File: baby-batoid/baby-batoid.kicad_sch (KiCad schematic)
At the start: 21 parts, among them J1 USB_C_Receptacle_USB2.0, U1 STM32F072CBT6, U2 PRTR5V0U2X, U3 XC6206PxxxMR-Regulator_Linear

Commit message: built baby batoid :D
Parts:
- added D1, D10, D11, D12, D13, D14, D15, D16, D17, D18, D19, D2, D20, D21, D22, D23, D24, D25, D26, D27, D28, D29, D3, D4, D5, D6, D7, D8, D9: D_Small, Diode_SMD:D_SOD-123, symbol Device:D_Small
- added MX1, MX10, MX11, MX12, MX13, MX14, MX15, MX16, MX17, MX18, MX19, MX2, MX20, MX21, MX22, MX23, MX24, MX25, MX26, MX27, MX28, MX29, MX3, MX4, MX5, MX6, MX7, MX8, MX9: MX_SW_HS, marbastlib-mx:SW_MX_HS_CPG151101S11_1u, symbol marbastlib-mx:MX_SW_HS_CPG151101S11
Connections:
- net A0 renamed ROW3
- net ROW3: now also D13.2 (A), D14.2 (A), D15.2 (A), D28.2 (A), D29.2 (A)
- net A1 renamed ROW2
- net ROW2: now also D10.2 (A), D11.2 (A), D12.2 (A), D24.2 (A), D25.2 (A), D26.2 (A), D27.2 (A), D9.2 (A)
- net A14 renamed COL4
- net COL4: now also MX16.1, MX20.1, MX24.1, MX28.1
- net A15 renamed COL5
- net COL5: now also MX17.1, MX21.1, MX25.1
- net B1 renamed COL0
- net COL0: now also MX1.1, MX14.1, MX5.1, MX9.1
- net B10 renamed COL2
- net COL2: now also MX11.1, MX15.1, MX3.1, MX7.1
- net B11 renamed COL3
- net COL3: now also MX12.1, MX13.1, MX4.1, MX8.1
- net B12 renamed ROW0
- net ROW0: now also D1.2 (A), D16.2 (A), D17.2 (A), D18.2 (A), D19.2 (A), D2.2 (A), D3.2 (A), D4.2 (A)
- net B13 renamed ROW1
- net ROW1: now also D20.2 (A), D21.2 (A), D22.2 (A), D23.2 (A), D5.2 (A), D6.2 (A), D7.2 (A), D8.2 (A)
- net B2 renamed COL1
- net COL1: now also MX10.1, MX2.1, MX6.1
- net B3 renamed COL6
- net COL6: now also MX18.1, MX22.1, MX26.1
- net B4 renamed COL7
- net COL7: now also MX19.1, MX23.1, MX27.1, MX29.1
- new net: D16.1 (K), MX16.2
- new net: D15.1 (K), MX15.2
- new net: D19.1 (K), MX19.2
- new net: D21.1 (K), MX21.2
- new net: D17.1 (K), MX17.2
- new net: D1.1 (K), MX1.2
- new net: D4.1 (K), MX4.2
- new net: D5.1 (K), MX5.2
- new net: D28.1 (K), MX28.2
- new net: D18.1 (K), MX18.2
- new net: D3.1 (K), MX3.2
- new net: D8.1 (K), MX8.2
- new net: D25.1 (K), MX25.2
- new net: D24.1 (K), MX24.2
- new net: D27.1 (K), MX27.2
- new net: D13.1 (K), MX13.2
- new net: D20.1 (K), MX20.2
- new net: D29.1 (K), MX29.2
- new net: D2.1 (K), MX2.2
- new net: D22.1 (K), MX22.2
- new net: D23.1 (K), MX23.2
- new net: D14.1 (K), MX14.2
- new net: D12.1 (K), MX12.2
- new net: D7.1 (K), MX7.2
- new net: D6.1 (K), MX6.2
- new net: D10.1 (K), MX10.2
- new net: D26.1 (K), MX26.2
- new net: D11.1 (K), MX11.2
- new net: D9.1 (K), MX9.2

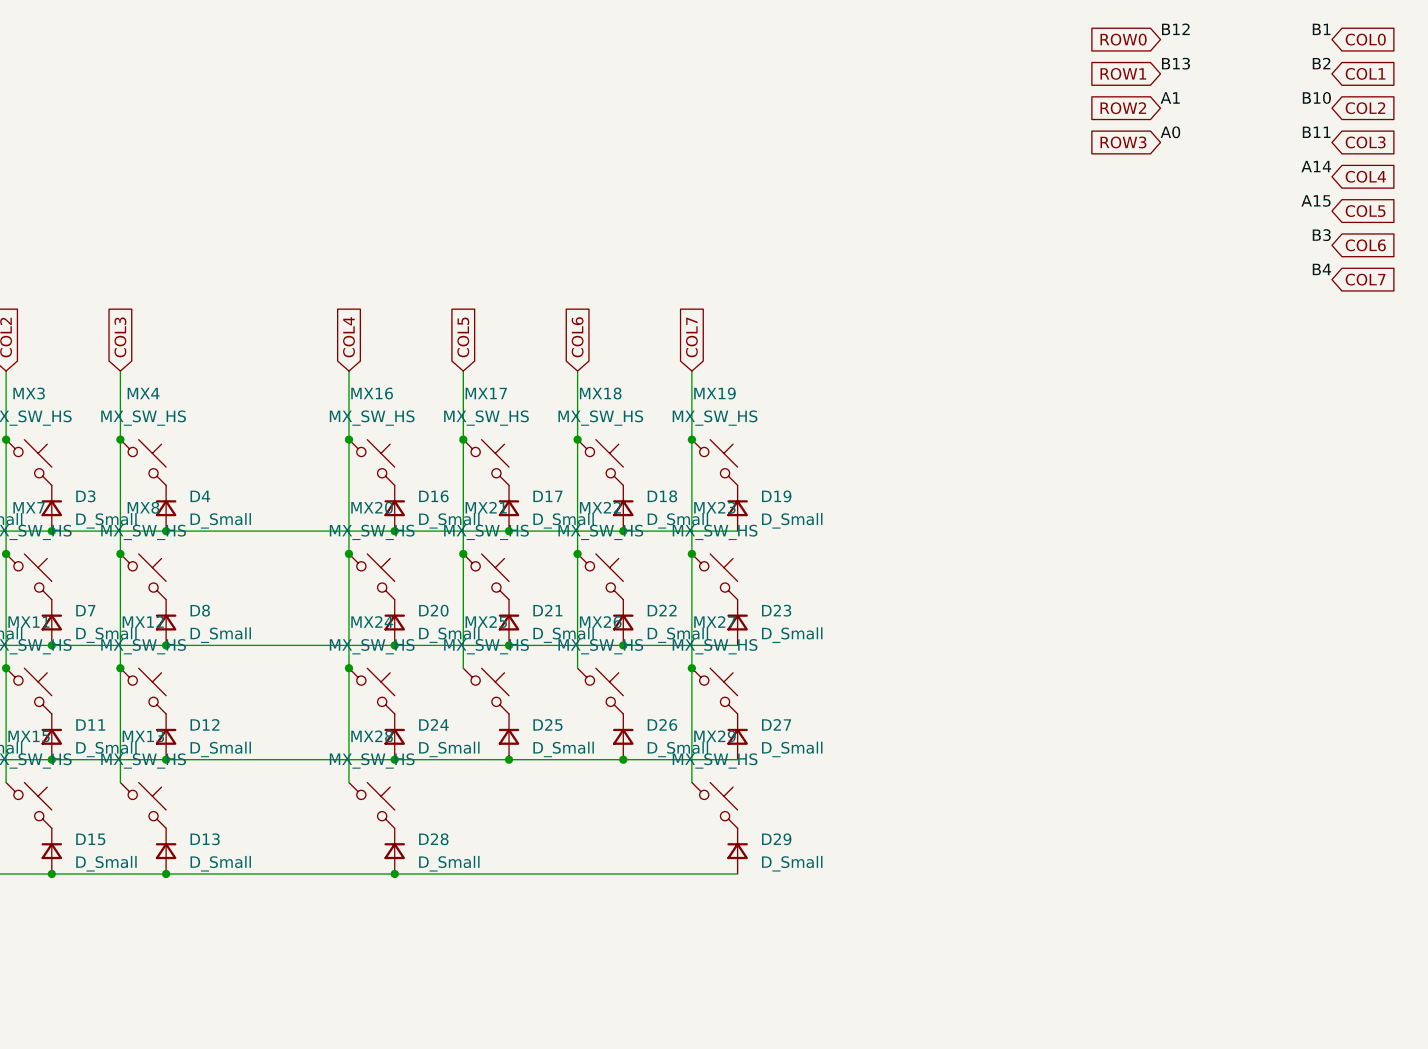
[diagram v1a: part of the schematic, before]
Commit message: cleaned up left routing, need to do right still
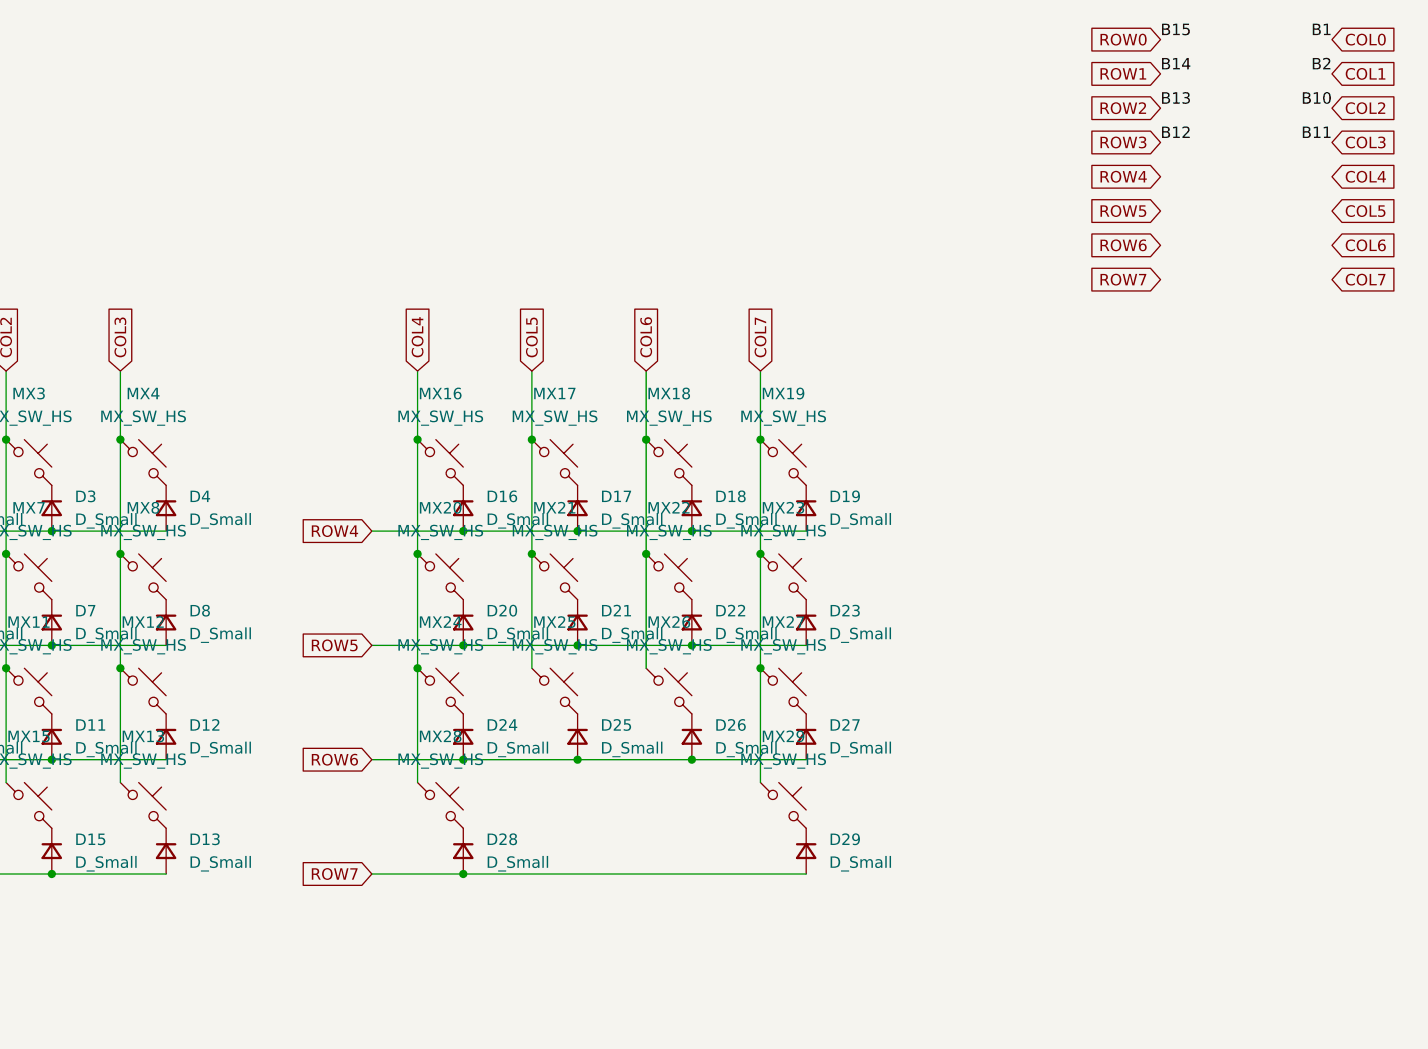
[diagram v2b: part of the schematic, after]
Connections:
- net B14 is gone; now on net ROW1: U1.27 (PB14)
- net B15 is gone; now on net ROW0: U1.28 (PB15)
- net COL4: no longer U1.37 (PA14)
- net COL5: no longer U1.38 (PA15)
- net COL6: no longer U1.39 (PB3)
- net COL7: no longer U1.40 (PB4)
- net ROW0: no longer D16.2 (A), D17.2 (A), D18.2 (A), D19.2 (A), U1.25 (PB12)
- net ROW1: no longer D20.2 (A), D21.2 (A), D22.2 (A), D23.2 (A), U1.26 (PB13)
- net ROW2: now also U1.26 (PB13); no longer D24.2 (A), D25.2 (A), D26.2 (A), D27.2 (A), U1.11 (PA1)
- net ROW3: now also U1.25 (PB12); no longer D28.2 (A), D29.2 (A), U1.10 (PA0)
- new net A0: U1.10 (PA0)
- new net A1: U1.11 (PA1)
- new net A14: U1.37 (PA14)
- new net A15: U1.38 (PA15)
- new net B3: U1.39 (PB3)
- new net B4: U1.40 (PB4)
- new net ROW4: D16.2 (A), D17.2 (A), D18.2 (A), D19.2 (A)
- new net ROW5: D20.2 (A), D21.2 (A), D22.2 (A), D23.2 (A)
- new net ROW6: D24.2 (A), D25.2 (A), D26.2 (A), D27.2 (A)
- new net ROW7: D28.2 (A), D29.2 (A)
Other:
- moved on the sheet: D16, D17, D18, D19, D20, D21, D22, D23, D24, D25, D26, D27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

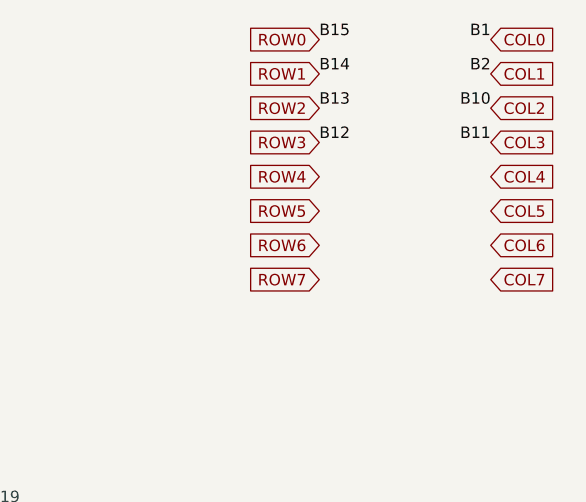
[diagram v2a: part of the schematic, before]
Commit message: finished cleaning routing up
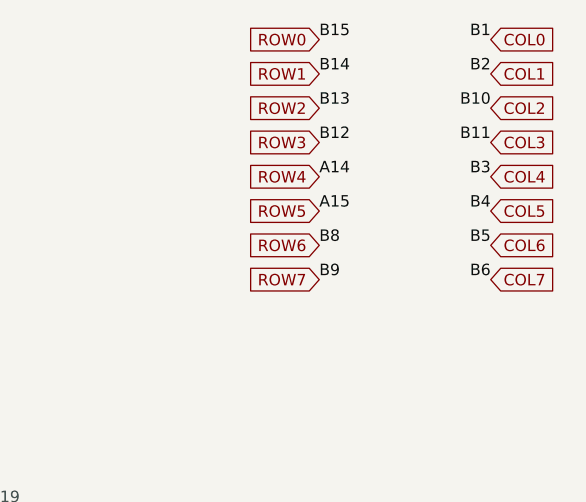
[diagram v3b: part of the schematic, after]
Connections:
- net A14 is gone; now on net ROW4: U1.37 (PA14)
- net A15 is gone; now on net ROW5: U1.38 (PA15)
- net B3 is gone; now on net COL4: U1.39 (PB3)
- net B4 is gone; now on net COL5: U1.40 (PB4)
- net B5 is gone; now on net COL6: U1.41 (PB5)
- net B6 is gone; now on net COL7: U1.42 (PB6)
- net B8 is gone; now on net ROW6: U1.45 (PB8)
- net B9 is gone; now on net ROW7: U1.46 (PB9)
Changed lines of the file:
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@@
+		)
+	)
+	(label "A15"
+		(at 317.5 31.75 0)
+		(effects
+			(font
+				(size 1.27 1.27)
+			)
+			(justify left bottom)
 		)
 	)
@@
 		)
 	)
+	(label "B8"
+		(at 317.5 35.56 0)
+		(effects
+			(font
+				(size 1.27 1.27)
+			)
+			(justify left bottom)
+		)
+	)
 	(label "B14"
 		(at 60.96 93.98 180)
@@
 		)
 	)
+	(label "B9"
+		(at 317.5 39.37 0)
+		(effects
+			(font
+				(size 1.27 1.27)
+			)
+			(justify left bottom)
+		)
+	)
 	(label "B8"
 		(at 60.96 78.74 180)
@@
 		)
 	)
+	(label "B4"
+		(at 336.55 31.75 180)
+		(effects
+			(font
+				(size 1.27 1.27)
+			)
+			(justify right bottom)
+		)
+	)
+	(label "B3"
+		(at 336.55 27.94 180)
+		(effects
+			(font
+				(size 1.27 1.27)
+			)
+			(justify right bottom)
+		)
+	)
 	(label "C14"
 		(at 60.325 50.8 180)
@@
 		)
 	)
+	(label "B6"
+		(at 336.55 39.37 180)
+		(effects
+			(font
+				(size 1.27 1.27)
+			)
+			(justify right bottom)
+		)
+	)
 	(label "C15"
 		(at 60.325 53.34 180)
@@
 		)
 	)
+	(label "A14"
+		(at 317.5 27.94 0)
+		(effects
+			(font
+				(size 1.27 1.27)
+			)
+			(justify left bottom)
+		)
+	)
 	(label "A5"
 		(at 98.425 43.18 0)
@@
 		(effects
 			(font
+				(size 1.27 1.27)
+			)
+			(justify right bottom)
+		)
+	)
+	(label "B5"
+		(at 336.55 35.56 180)
+		(effects
+			(font
